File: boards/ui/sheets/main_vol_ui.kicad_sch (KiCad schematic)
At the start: 4 parts

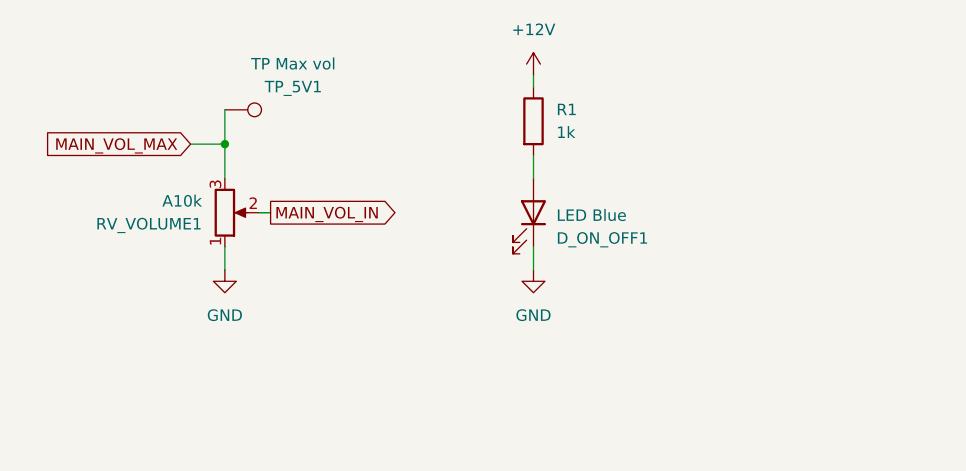
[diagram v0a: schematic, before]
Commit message: Replaced wired MIDI connection to pins
https://github.com/shmoergh/hog/issues/32

MIDI connection was done with manual wired NTS connectors. Now they are replaced with pins and pinheaders just like the other boards.
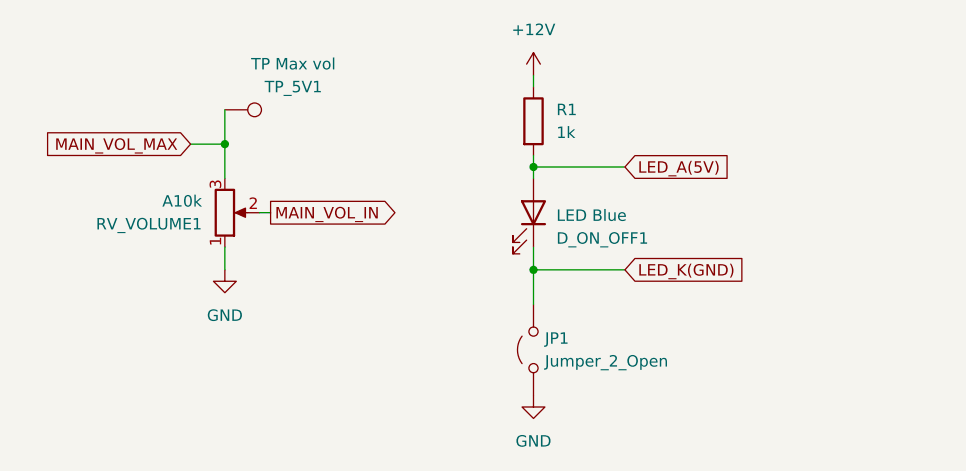
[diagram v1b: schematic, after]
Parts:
- added JP1: Jumper_2_Open, Jumper:SolderJumper-2_P1.3mm_Bridged_Pad1.0x1.5mm, symbol Jumper:Jumper_2_Open
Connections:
- net GND: now also JP1.1 (A); no longer D_ON_OFF1.1 (K)
- net LED_A(5V): now reaches D_ON_OFF1.2 (A), R1.2
- new net LED_K(GND): D_ON_OFF1.1 (K), JP1.2 (B)
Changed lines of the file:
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@@
 	(paper "A4")
+	(junction
+		(at 158.75 106.68)
+		(diameter 0)
+		(color 0 0 0 0)
+	)
 	(junction
 		(at 124.46 92.71)
@@
 		(color 0 0 0 0)
 	)
+	(junction
+		(at 158.75 95.25)
+		(diameter 0)
+		(color 0 0 0 0)
+	)
 	(wire
 		(pts
@@
 	(wire
 		(pts
+			(xy 158.75 95.25) (xy 168.91 95.25)
+		)
+		(stroke
+			(width 0)
+			(type default)
+		)
+	)
+	(wire
+		(pts
 			(xy 124.46 88.9) (xy 124.46 92.71)
 		)
@@
 	(wire
 		(pts
+			(xy 158.75 106.68) (xy 168.91 106.68)
+		)
+		(stroke
+			(width 0)
+			(type default)
+		)
+	)
+	(wire
+		(pts
 			(xy 158.75 104.14) (xy 158.75 106.68)
 		)
@@
 	(wire
 		(pts
-			(xy 158.75 93.98) (xy 158.75 96.52)
+			(xy 158.75 95.25) (xy 158.75 96.52)
+		)
+		(stroke
+			(width 0)
+			(type default)
+		)
+	)
+	(wire
+		(pts
+			(xy 158.75 93.98) (xy 158.75 95.25)
 		)
 		(stroke
@@
 			(width 0)
 			(type default)
+		)
+	)
+	(wire
+		(pts
+			(xy 158.75 110.49) (xy 158.75 106.68)
+		)
+		(stroke
+			(width 0)
+			(type default)
+		)
+	)
+	(global_label "LED_A(5V)"
+		(shape input)
+		(at 168.91 95.25 0)
+		(fields_autoplaced yes)
+		(effects
+			(font
+				(size 1.27 1.27)
+			)
+			(justify left)
+		)
+		(property "Intersheetrefs" "${INTERSHEET_REFS}"
+			(at 181.39 95.25 0)
+			(effects
+				(font
+					(size 1.27 1.27)
+				)
+				(justify left)
+				(hide yes)
+			)
 		)
 	)
@@
 				)
 				(justify right)
+				(hide yes)
+			)
+		)
+	)
+	(global_label "LED_K(GND)"
+		(shape input)
+		(at 168.91 106.68 0)
+		(fields_autoplaced yes)
+		(effects
+			(font
+				(size 1.27 1.27)
+			)
+			(justify left)
+		)
+		(property "Intersheetrefs" "${INTERSHEET_REFS}"
+			(at 183.1438 106.68 0)
+			(effects
+				(font
+					(size 1.27 1.27)
+				)
+				(justify left)
 				(hide yes)
 			)
@@
 	(symbol
 		(lib_id "power:GND")
-		(at 158.75 106.68 0)
+		(at 158.75 120.65 0)
 		(unit 1)
 		(exclude_from_sim no)
@@
 		(fields_autoplaced yes)
 		(property "Reference" "#PWR02"
-			(at 158.75 113.03 0)
+			(at 158.75 127 0)
 			(effects
 				(font
@@
 		)
 		(property "Value" "GND"
-			(at 158.75 111.76 0)
+			(at 158.75 125.73 0)
 			(effects
 				(font
@@
 		)
 		(property "Footprint" ""
-			(at 158.75 106.68 0)
+			(at 158.75 120.65 0)
 			(effects
 				(font
@@
 		)
 		(property "Datasheet" ""
-			(at 158.75 106.68 0)
+			(at 158.75 120.65 0)
 			(effects
 				(font
@@
 		)
 		(property "Description" ""
-			(at 158.75 106.68 0)
+			(at 158.75 120.65 0)
 			(effects
 				(font
@@
 					(unit 1)
 				)
+			)
+		)
+	)
+	(symbol
+		(lib_id "Jumper:Jumper_2_Open")
+		(at 158.75 115.57 90)
+		(unit 1)
+		(exclude_from_sim yes)
+		(in_bom yes)
+		(on_board yes)
+		(dnp no)
+		(fields_autoplaced yes)
+		(property "Reference" "JP1"
+			(at 160.02 114.2999 90)
+			(effects
+				(font
+					(size 1.27 1.27)
+				)
+				(justify right)
+			)
+		)
+		(property "Value" "Jumper_2_Open"
+			(at 160.02 116.8399 90)
+			(effects
+				(font
+					(size 1.27 1.27)
+				)
+				(justify right)
+			)
+		)
+		(property "Footprint" "Jumper:SolderJumper-2_P1.3mm_Bridged_Pad1.0x1.5mm"
+			(at 158.75 115.57 0)
+			(effects
+				(font
+					(size 1.27 1.27)
+				)
+				(hide yes)
+			)
+		)
+		(property "Datasheet" "~"
+			(at 158.75 115.57 0)
+			(effects
+				(font
+					(size 1.27 1.27)
+				)
+				(hide yes)
+			)
+		)
+		(property "Description" "Jumper, 2-pole, open"
+			(at 158.75 115.57 0)
+			(effects
+				(font
+					(size 1.27 1.27)
+				)
+				(hide yes)
+			)
+		)
+		(pin "1"
+		)
+		(pin "2"
+		)
+		(instances
+			(project ""
+				(path "/639b6cfb-11bc-4acb-8020-87e420d3f12c/953ce80c-6ceb-4933-9c61-bce393d8a016"
+					(reference "JP1")
+					(unit 1)
+				)

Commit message: Added production files for the UI board
ref https://github.com/shmoergh/hog/issues/19
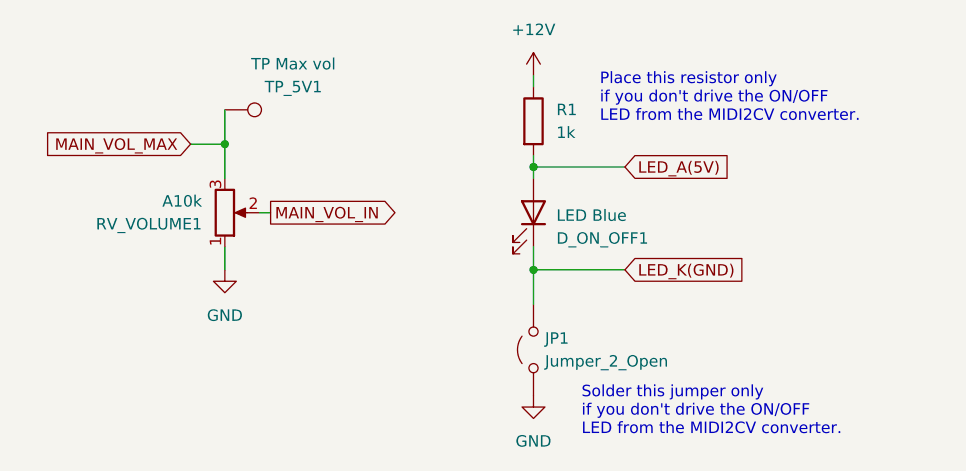
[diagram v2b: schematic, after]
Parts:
- D_ON_OFF1: Part No. (none) -> 859-LTL-1CHG; Part URL (none) -> https://mou.sr/3OXMWKk; Vendor (none) -> Mouser
- R1: Part No. (none) -> 303-MF0W4FF1001A10; Part URL (none) -> https://mou.sr/3ZUsGjh; Vendor (none) -> Mouser
- RV_VOLUME1: Part No. (none) -> 652-PTV09A4025FA103; Part URL (none) -> https://mou.sr/4bCOV0e; Vendor (none) -> Mouser
- TP_5V1: now left out of the parts list
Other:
- note added: "Place this resistor only if you don't drive the ON/OFF LED from the MIDI2CV converter."
- note added: "Solder this jumper only if you don't drive the ON/OFF LED from the MIDI2CV converter."
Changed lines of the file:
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@@
+		)
+	)
+	(text "Place this resistor only\nif you don't drive the ON/OFF\nLED from the MIDI2CV converter."
+		(exclude_from_sim no)
+		(at 166.116 87.63 0)
+		(effects
+			(font
+				(size 1.27 1.27)
+			)
+			(justify left)
+		)
+	)
+	(text "Solder this jumper only\nif you don't drive the ON/OFF\nLED from the MIDI2CV converter."
+		(exclude_from_sim no)
+		(at 164.084 122.428 0)
+		(effects
+			(font
+				(size 1.27 1.27)
+			)
+			(justify left)
 		)
 	)
@@
 			)
 		)
+		(property "Part No." "303-MF0W4FF1001A10 "
+			(at 158.75 90.17 0)
+			(effects
+				(font
+					(size 1.27 1.27)
+				)
+				(hide yes)
+			)
+		)
+		(property "Part URL" "https://mou.sr/3ZUsGjh"
+			(at 158.75 90.17 0)
+			(effects
+				(font
+					(size 1.27 1.27)
+				)
+				(hide yes)
+			)
+		)
+		(property "Vendor" "Mouser"
+			(at 158.75 90.17 0)
+			(effects
+				(font
+					(size 1.27 1.27)
+				)
+				(hide yes)
+			)
+		)
+		(property "LCSC" ""
+			(at 158.75 90.17 0)
+			(effects
+				(font
+					(size 1.27 1.27)
+				)
+				(hide yes)
+			)
+		)
 		(pin "1"
 		)
@@
 		(unit 1)
 		(exclude_from_sim no)
-		(in_bom yes)
+		(in_bom no)
 		(on_board yes)
 		(dnp no)
@@
 		)
 		(property "Description" ""
+			(at 124.46 88.9 0)
+			(effects
+				(font
+					(size 1.27 1.27)
+				)
+				(hide yes)
+			)
+		)
+		(property "Part No." ""
+			(at 124.46 88.9 0)
+			(effects
+				(font
+					(size 1.27 1.27)
+				)
+				(hide yes)
+			)
+		)
+		(property "Part URL" ""
+			(at 124.46 88.9 0)
+			(effects
+				(font
+					(size 1.27 1.27)
+				)
+				(hide yes)
+			)
+		)
+		(property "Vendor" ""
+			(at 124.46 88.9 0)
+			(effects
+				(font
+					(size 1.27 1.27)
+				)
+				(hide yes)
+			)
+		)
+		(property "LCSC" ""
 			(at 124.46 88.9 0)
 			(effects
@@
 			)
 		)
+		(property "Part No." "859-LTL-1CHG "
+			(at 158.75 100.33 0)
+			(effects
+				(font
+					(size 1.27 1.27)
+				)
+				(hide yes)
+			)
+		)
+		(property "Part URL" "https://mou.sr/3OXMWKk"
+			(at 158.75 100.33 0)
+			(effects
+				(font
+					(size 1.27 1.27)
+				)
+				(hide yes)
+			)
+		)
+		(property "Vendor" "Mouser"
+			(at 158.75 100.33 0)
+			(effects
+				(font
+					(size 1.27 1.27)
+				)
+				(hide yes)
+			)
+		)
+		(property "LCSC" ""
+			(at 158.75 100.33 0)
+			(effects
+				(font
+					(size 1.27 1.27)
+				)
+				(hide yes)
+			)
+		)
 		(pin "1"
 		)
@@
 			(at 124.46 100.33 0)
 			(effects
+				(font
+					(size 1.27 1.27)
+				)
+				(hide yes)
+			)
+		)
+		(property "Part No." "652-PTV09A4025FA103 "
+			(at 124.46 100.33 0)
+			(effects
+				(font
+					(size 1.27 1.27)
+				)
+				(hide yes)
+			)
+		)
+		(property "Part URL" "https://mou.sr/4bCOV0e"
+			(at 124.46 100.33 0)
+			(effects
+				(font
+					(size 1.27 1.27)
+				)
+				(hide yes)
+			)
+		)
+		(property "Vendor" "Mouser"
+			(at 124.46 100.33 0)
+			(effects
+				(font
+					(size 1.27 1.27)
+				)
+				(hide yes)
+			)
+		)
+		(property "LCSC" ""
+			(at 124.46 100.33 0)
+			(effects

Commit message: Updated resistor Mouser no's and added full bom
- Some of the THT resistors in the BOM were referencing to products with min. 1000 pcs order quantity
- Added a full Mouser BOM which can be used to order all Mouser components by uploading to their BOM tool: https://hu.mouser.com/bom/
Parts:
- R1: Part No. 303-MF0W4FF1001A10 -> 603-MFR-25FBF52-1K; Part URL https://mou.sr/3ZUsGjh -> https://mou.sr/43MmrAb
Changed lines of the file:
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@@
 			)
 		)
-		(property "Part No." "303-MF0W4FF1001A10 "
+		(property "Part No." "603-MFR-25FBF52-1K "
 			(at 158.75 90.17 0)
 			(effects
@@
 			)
 		)
-		(property "Part URL" "https://mou.sr/3ZUsGjh"
+		(property "Part URL" "https://mou.sr/43MmrAb"
 			(at 158.75 90.17 0)
 			(effects
